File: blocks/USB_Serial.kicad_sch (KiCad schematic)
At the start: 5 parts, among them U301 FT232RL

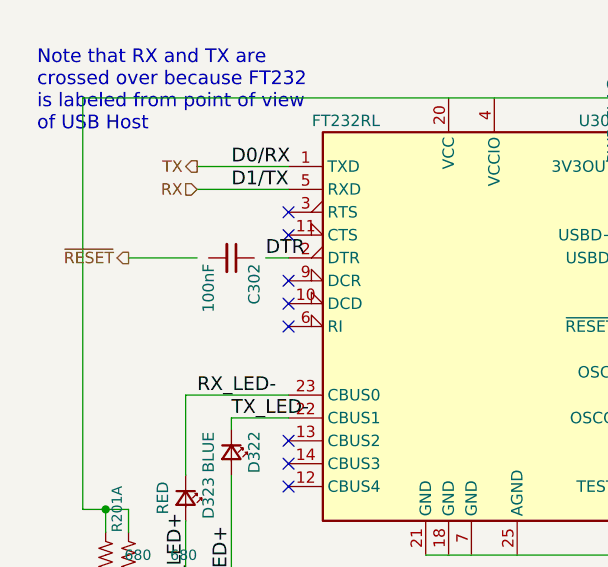
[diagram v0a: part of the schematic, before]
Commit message: Corrected capacitor which should have been connected but wasn't
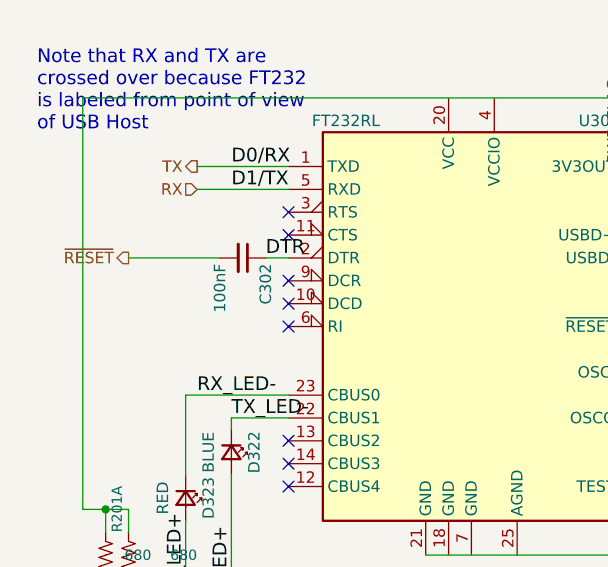
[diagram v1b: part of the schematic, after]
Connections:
- net DTR: now also C302.1
- net ~{RESET}: now also C302.2
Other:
- moved on the sheet: C302
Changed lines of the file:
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@@
     (stroke (width 0) (type default))
   )
-  (wire (pts (xy 110.49 85.09) (xy 118.11 85.09))
+  (wire (pts (xy 110.49 85.09) (xy 120.65 85.09))
     (stroke (width 0) (type default))
   )
@@
     )
   )
-  (symbol (lib_id "Device:C_Small") (at 121.92 85.09 270) (unit 1)
+  (symbol (lib_id "Device:C_Small") (at 123.19 85.09 270) (unit 1)
     (in_bom yes) (on_board yes) (dnp no)
-    (property "Reference" "C302" (at 124.46 85.725 0)
+    (property "Reference" "C302" (at 125.73 85.725 0)
       (effects (font (size 1.27 1.27)) (justify left))
     )
-    (property "Value" "100nF" (at 119.38 85.725 0)
+    (property "Value" "100nF" (at 120.65 85.725 0)
       (effects (font (size 1.27 1.27)) (justify left))
     )
-    (property "Footprint" "Capacitor_SMD:C_0402_1005Metric" (at 121.92 85.09 0)
+    (property "Footprint" "Capacitor_SMD:C_0402_1005Metric" (at 123.19 85.09 0)
       (effects (font (size 1.27 1.27)) hide)
     )
-    (property "Datasheet" "~" (at 121.92 85.09 0)
+    (property "Datasheet" "~" (at 123.19 85.09 0)
       (effects (font (size 1.27 1.27)) hide)
     )
